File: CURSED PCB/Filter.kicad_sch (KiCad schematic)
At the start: 5 parts, among them U8 LTC2066

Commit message: component fixes
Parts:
- C17: value 1u -> 1n
- C18: value 1u -> 430pF
- R10: value 11.7k -> 46.7k
- R11: value 21k -> 103k
- U8: value LTC2066 -> LT6023
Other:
- note added: "Math is done on a google sheets labbeled "Experimental & PCB Data Setup Master" under AA Filter"
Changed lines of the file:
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@@
 	(generator_version "9.0")
 	(paper "A4")
+	(text "Math is done on a google sheets labbeled \"Experimental & PCB Data Setup Master\" under AA Filter\n"
+		(exclude_from_sim no)
+		(at 94.996 127 0)
+		(effects
+			(font
+				(size 1.27 1.27)
+			)
+		)
+	)
 	(text "Reference sheet:\nhttps://ez.analog.com/cfs-filesystemfile/__key/communityserver-wikis-components-files/00-00-00-06-97/KWIK_5F00_FAQ-_2D00_-Design-of-an-anti_2D00_aliasing-Sallen_2D00_Key-filter.pdf?_=638128614376877068"
 		(exclude_from_sim no)
@@
 			)
 		)
-		(property "Value" "1u"
+		(property "Value" "1n"
 			(at 82.5563 72.39 90)
 			(effects
@@
 			)
 		)
-		(property "Value" "1u"
+		(property "Value" "430pF"
 			(at 93.98 110.4962 0)
 			(effects
@@
 			)
 		)
-		(property "Value" "11.7k"
+		(property "Value" "46.7k"
 			(at 64.77 96.52 90)
 			(effects
@@
 			)
 		)
-		(property "Value" "21k"
+		(property "Value" "103k"
 			(at 81.28 96.52 90)
 			(effects
@@
 			)
 		)
-		(property "Value" "LTC2066"
+		(property "Value" "LT6023"
 			(at 123.19 92.456 0)
 			(effects

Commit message: text for reviwers
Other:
- note added: "Math is done on a google sheets labbeled "Experimental & PCB Data Setup Master" under AA Filter Google sheet is found under payload 2026 under data magnement"
- note removed: "Math is done on a google sheets labbeled "Experimental & PCB Data Setup Master" under AA Filter"
- note removed: "Reference sheet: https://ez.analog.com/cfs-filesystemfile/__key/communityserver-wikis-components-files/00-00-00-06-97/KWIK_5F00_FAQ-_2D00_-Design-of-an-anti_2D00_aliasing-Sallen_2D00_Key-filter.pdf?_=638128614376877068"
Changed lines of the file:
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@@
 	(generator_version "9.0")
 	(paper "A4")
-	(text "Math is done on a google sheets labbeled \"Experimental & PCB Data Setup Master\" under AA Filter\n"
+	(text "Math is done on a google sheets labbeled \"Experimental & PCB Data Setup Master\" under AA Filter\nGoogle sheet is found under payload 2026 under data magnement "
 		(exclude_from_sim no)
 		(at 94.996 127 0)
@@
 		)
 	)
-	(text "Reference sheet:\nhttps://ez.analog.com/cfs-filesystemfile/__key/communityserver-wikis-components-files/00-00-00-06-97/KWIK_5F00_FAQ-_2D00_-Design-of-an-anti_2D00_aliasing-Sallen_2D00_Key-filter.pdf?_=638128614376877068"
-		(exclude_from_sim no)
-		(at 61.976 17.526 0)
-		(effects
-			(font
-				(size 1.27 1.27)
-			)
-			(justify left)
-		)
-	)

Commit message: fix
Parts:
- C17: value 1n -> 47nF
- C18: value 430pF -> 20nF
- R10: value 46.7k -> 986
- R11: value 103k -> 2.23k
- U8: value LT6023 -> LT6233
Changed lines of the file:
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@@
 			)
 		)
-		(property "Value" "1n"
+		(property "Value" "47nF"
 			(at 82.5563 72.39 90)
 			(effects
@@
 			)
 		)
-		(property "Value" "430pF"
+		(property "Value" "20nF"
 			(at 93.98 110.4962 0)
 			(effects
@@
 			)
 		)
-		(property "Value" "46.7k"
+		(property "Value" "986"
 			(at 64.77 96.52 90)
 			(effects
@@
 			)
 		)
-		(property "Value" "103k"
+		(property "Value" "2.23k"
 			(at 81.28 96.52 90)
 			(effects
@@
 			)
 		)
-		(property "Value" "LT6023"
+		(property "Value" "LT6233"
 			(at 123.19 92.456 0)
 			(effects

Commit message: schematic changes
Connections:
- net +5V renamed +3.3VD
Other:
- note added: "These values are subject to change in expected freq changes"
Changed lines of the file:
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@@
+		)
+	)
+	(text "These values are subject to change in expected freq changes"
+		(exclude_from_sim no)
+		(at 40.132 81.026 0)
+		(effects
+			(font
+				(size 1.27 1.27)
+			)
 		)
 	)
@@
 	(wire
 		(pts
+			(xy 102.87 69.85) (xy 102.87 91.44)
+		)
+		(stroke
+			(width 0)
+			(type default)
+		)
+	)
+	(wire
+		(pts
 			(xy 91.44 100.33) (xy 91.44 106.68)
-		)
-		(stroke
-			(width 0)
-			(type default)
-		)
-	)
-	(wire
-		(pts
-			(xy 102.87 69.85) (xy 102.87 91.44)
 		)
 		(stroke
@@
 	)
 	(symbol
+		(lib_id "power:+3.3VA")
+		(at 102.87 69.85 0)
+		(unit 1)
+		(exclude_from_sim no)
+		(in_bom yes)
+		(on_board yes)
+		(dnp no)
+		(fields_autoplaced yes)
+		(property "Reference" "#PWR046"
+			(at 102.87 73.66 0)
+			(effects
+				(font
+					(size 1.27 1.27)
+				)
+				(hide yes)
+			)
+		)
+		(property "Value" "+3.3VD"
+			(at 105.41 68.5799 0)
+			(effects
+				(font
+					(size 1.27 1.27)
+				)
+				(justify left)
+			)
+		)
+		(property "Footprint" ""
+			(at 102.87 69.85 0)
+			(effects
+				(font
+					(size 1.27 1.27)
+				)
+				(hide yes)
+			)
+		)
+		(property "Datasheet" ""
+			(at 102.87 69.85 0)
+			(effects
+				(font
+					(size 1.27 1.27)
+				)
+				(hide yes)
+			)
+		)
+		(property "Description" "Power symbol creates a global label with name \"+3.3VA\""
+			(at 102.87 69.85 0)
+			(effects
+				(font
+					(size 1.27 1.27)
+				)
+				(hide yes)
+			)
+		)
+		(pin "1"
+		)
+		(instances
+			(project "sensor_1"
+				(path "/9fb1a86f-679c-4b88-9ed1-932f4f414580/543706d6-8cb0-4c51-81f6-888765ec3907/1dbad184-dd5f-4b28-bd02-77889e07b3d7"
+					(reference "#PWR046")
+					(unit 1)
+				)
+			)
+		)
+	)
+	(symbol
 		(lib_id "power:GND")
 		(at 102.87 111.76 0)
@@
 					(unit 1)
 				)
-			)
-		)
-	)
-	(symbol
-		(lib_id "power:+5V")
-		(at 102.87 69.85 0)
-		(unit 1)
-		(exclude_from_sim no)
-		(in_bom yes)
-		(on_board yes)
-		(dnp no)
-		(fields_autoplaced yes)
-		(property "Reference" "#PWR046"
-			(at 102.87 73.66 0)
-			(effects
-				(font
-					(size 1.27 1.27)
-				)
-				(hide yes)
-			)
-		)
-		(property "Value" "+5V"
-			(at 102.87 64.77 0)
-			(effects
-				(font
-					(size 1.27 1.27)
-				)
-			)
-		)
-		(property "Footprint" ""
-			(at 102.87 69.85 0)
-			(effects
-				(font
-					(size 1.27 1.27)
-				)
-				(hide yes)
-			)
-		)
-		(property "Datasheet" ""
-			(at 102.87 69.85 0)
-			(effects
-				(font
-					(size 1.27 1.27)
-				)
-				(hide yes)
-			)
-		)
-		(property "Description" "Power symbol creates a global label with name \"+5V\""
-			(at 102.87 69.85 0)
-			(effects
-				(font
-					(size 1.27 1.27)
-				)
-				(hide yes)
-			)
-		)
-		(pin "1"
-		)
-		(instances
-			(project ""
-				(path "/9fb1a86f-679c-4b88-9ed1-932f4f414580/543706d6-8cb0-4c51-81f6-888765ec3907/1dbad184-dd5f-4b28-bd02-77889e07b3d7"
-					(reference "#PWR046")
-					(unit 1)
-				)

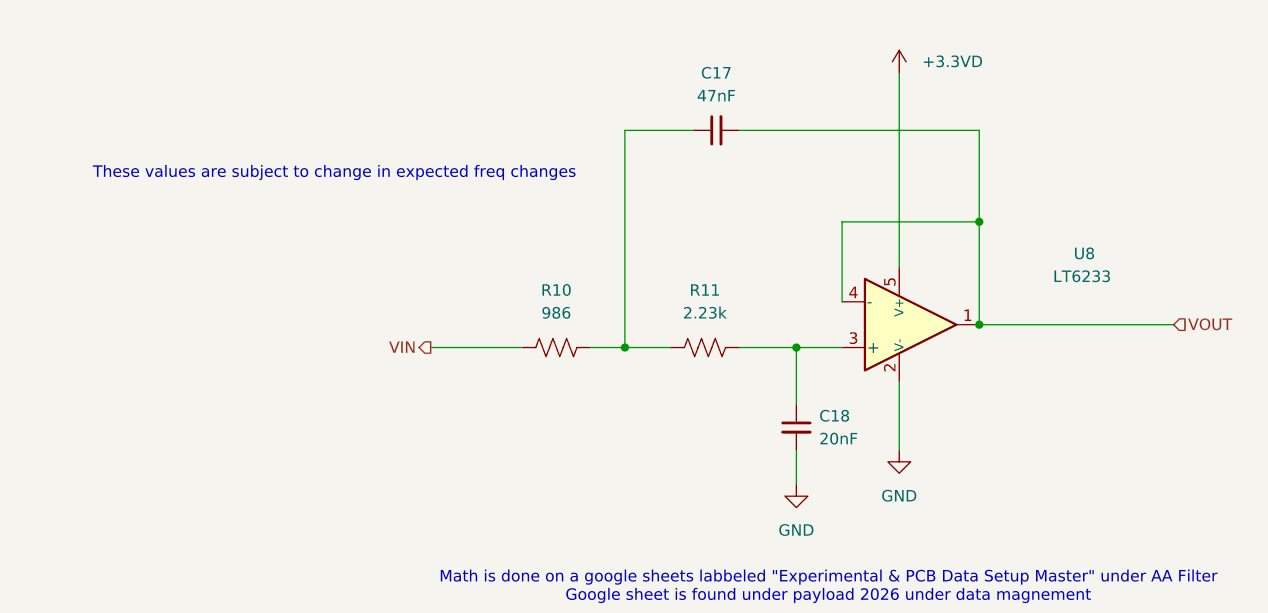
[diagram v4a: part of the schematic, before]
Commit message: footprint folde rupdate
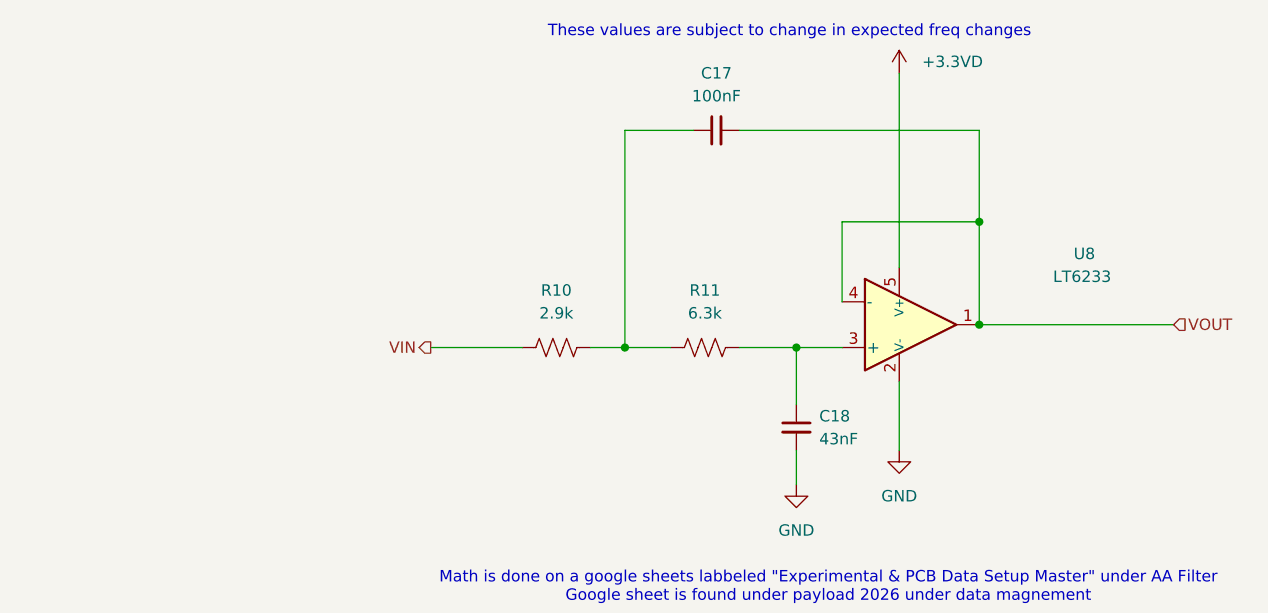
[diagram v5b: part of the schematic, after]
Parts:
- C17: value 47nF -> 100nF
- C18: value 20nF -> 43nF
- R10: value 986 -> 2.9k
- R11: value 2.23k -> 6.3k
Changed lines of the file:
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@@
 	(text "These values are subject to change in expected freq changes"
 		(exclude_from_sim no)
-		(at 40.132 81.026 0)
+		(at 90.678 65.278 0)
 		(effects
 			(font
@@
 			)
 		)
-		(property "Value" "47nF"
+		(property "Value" "100nF"
 			(at 82.5563 72.39 90)
 			(effects
@@
 			)
 		)
-		(property "Value" "20nF"
+		(property "Value" "43nF"
 			(at 93.98 110.4962 0)
 			(effects
@@
 			)
 		)
-		(property "Value" "986"
+		(property "Value" "2.9k"
 			(at 64.77 96.52 90)
 			(effects
@@
 			)
 		)
-		(property "Value" "2.23k"
+		(property "Value" "6.3k"
 			(at 81.28 96.52 90)
 			(effects

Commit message: temp circuit update
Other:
- note removed: "These values are subject to change in expected freq changes"
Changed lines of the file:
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@@
-		)
-	)
-	(text "These values are subject to change in expected freq changes"
-		(exclude_from_sim no)
-		(at 90.678 65.278 0)
-		(effects
-			(font
-				(size 1.27 1.27)
-			)
 		)
 	)
